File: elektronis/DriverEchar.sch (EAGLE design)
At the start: 27 parts, among them IC1 7805T, IC2 L293D

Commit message: update komponen
menambah tactile switch / micro switch
pembaharuan pelabelan komponen
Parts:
- removed JP1: (no value), pinhead:PINHD-1X2
- removed S2: (no value), switch:320-916
- added JP14, SPWR: (no value), pinhead:PINHD-1X3
- added U$2, U$3: MICROSWITCH_2X3, custom:MICROSWITCH_2X3
- renumbered JP10 to D2, JP11 to D3, JP12 to D4, JP13 to D5, JP2 to A3, JP3 to IC2_LCD, JP7 to A1, JP9 to SERIAL_DATA
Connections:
- new net VIN: POWERIN.2, SPWR.1, U$3.COM1
- net 5V: now also JP14.2, U$2.NC1; no longer S2.O
- net VBAT: now also JP14.3, SPWR.2, U$2.NO1, U$3.NO1; no longer POWERIN.2, S2.S
- net VM: now also JP14.1, U$2.COM1; no longer S2.P
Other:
- moved on the sheet: POWERIN

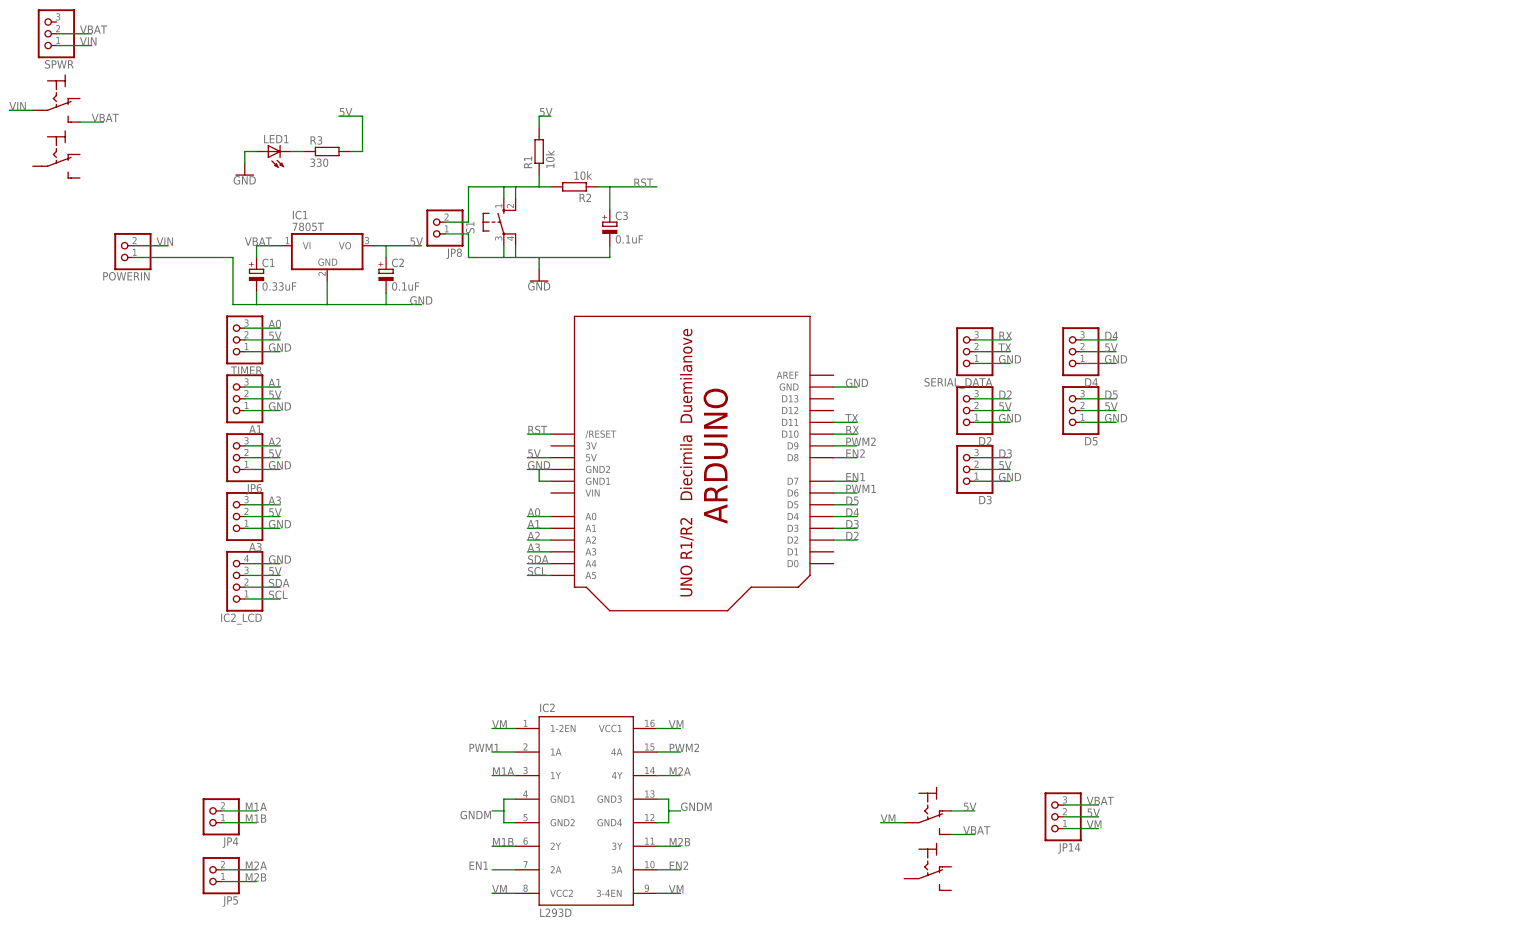
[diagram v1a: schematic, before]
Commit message: fix jumper and pin header space
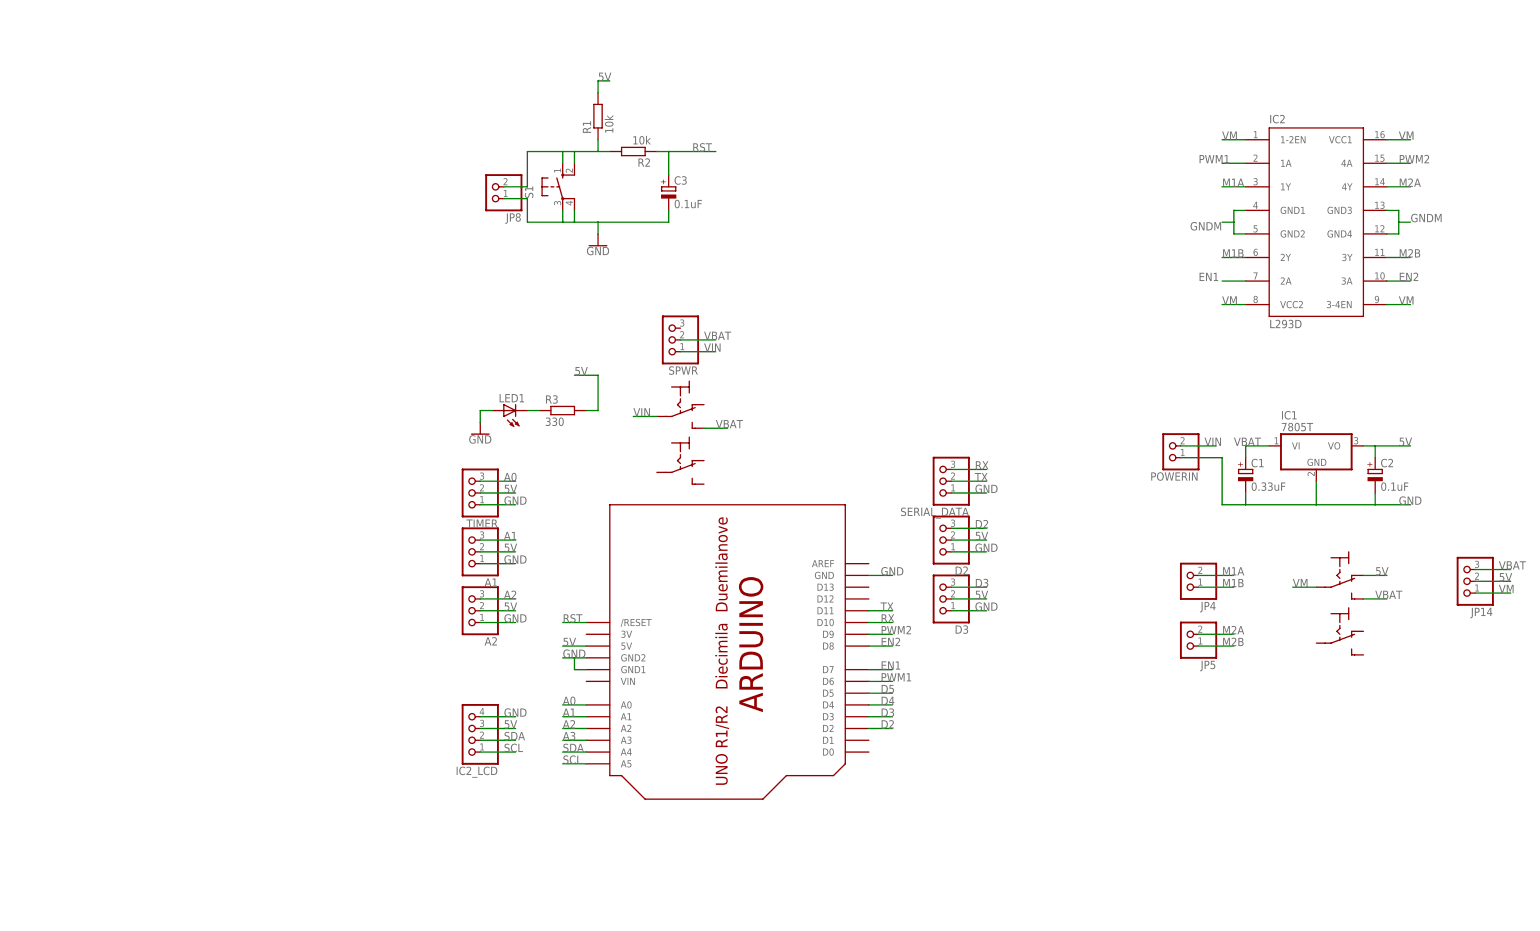
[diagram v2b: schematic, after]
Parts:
- removed A3, D4, D5, JP6: (no value), pinhead:PINHD-1X3
- added A2: (no value), pinhead:PINHD-1X3
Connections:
- net 5V: now also A2.2; no longer A3.2, D4.2, D5.2, JP6.2
- net A2: now also A2.3; no longer JP6.3
- net A3: no longer A3.3
- net D4: no longer D4.3
- net D5: no longer D5.3
- net GND: now also A2.1; no longer A3.1, D4.1, D5.1, JP6.1
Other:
- moved on the sheet: A1, C1, C2, C3, D2, D3, IC1, IC2, IC2_LCD, JP14, JP4, JP5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
